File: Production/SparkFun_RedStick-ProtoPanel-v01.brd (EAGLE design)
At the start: 137.2 x 153.2 mm, 495 parts, among them Q1 DMG2307L, Q10 MOSFET-NCHANNEL2N7002PW, Q11 DMG2307L, Q12 MOSFET-NCHANNEL2N7002PW, Q13 DMG2307L, Q14 MOSFET-NCHANNEL2N7002PW, Q15 DMG2307L, Q16 MOSFET-NCHANNEL2N7002PW, Q17 DMG2307L, Q18 MOSFET-NCHANNEL2N7002PW, Q19 DMG2307L, Q2 MOSFET-NCHANNEL2N7002PW, Q20 MOSFET-NCHANNEL2N7002PW, Q21 DMG2307L, Q22 MOSFET-NCHANNEL2N7002PW, Q23 DMG2307L, Q24 MOSFET-NCHANNEL2N7002PW, Q3 DMG2307L, Q4 MOSFET-NCHANNEL2N7002PW, Q5 DMG2307L, Q6 MOSFET-NCHANNEL2N7002PW, Q7 DMG2307L, Q8 MOSFET-NCHANNEL2N7002PW, Q9 DMG2307L, U1 FTS31XS-U, U10 ATMEGA328P_TQFP, U11 5.0v, U12 FTS31XS-U, U13 ATMEGA328P_TQFP, U14 5.0v, U15 FTS31XS-U, U16 ATMEGA328P_TQFP, U17 5.0v, U18 FTS31XS-U, U19 ATMEGA328P_TQFP, U2 ATMEGA328P_TQFP, U20 5.0v, U21 FTS31XS-U, U22 ATMEGA328P_TQFP, U23 5.0v, U24 FTS31XS-U, U25 ATMEGA328P_TQFP, U26 5.0v, U27 FTS31XS-U, U28 ATMEGA328P_TQFP, U29 5.0v, U3 ATMEGA328P_TQFP, U30 FTS31XS-U, U31 ATMEGA328P_TQFP, U32 5.0v, U33 FTS31XS-U, U34 ATMEGA328P_TQFP, U35 5.0v, U36 FTS31XS-U, U4 5.0v, U5 5.0v, U6 FTS31XS-U, U7 ATMEGA328P_TQFP, U8 5.0v, U9 FTS31XS-U, Y1 16MHZ, Y10 16MHZ, Y11 16MHZ, Y12 16MHZ, Y2 16MHZ, Y3 16MHZ, Y4 16MHZ, Y5 16MHZ, Y6 16MHZ, Y7 16MHZ, Y8 16MHZ, Y9 16MHZ

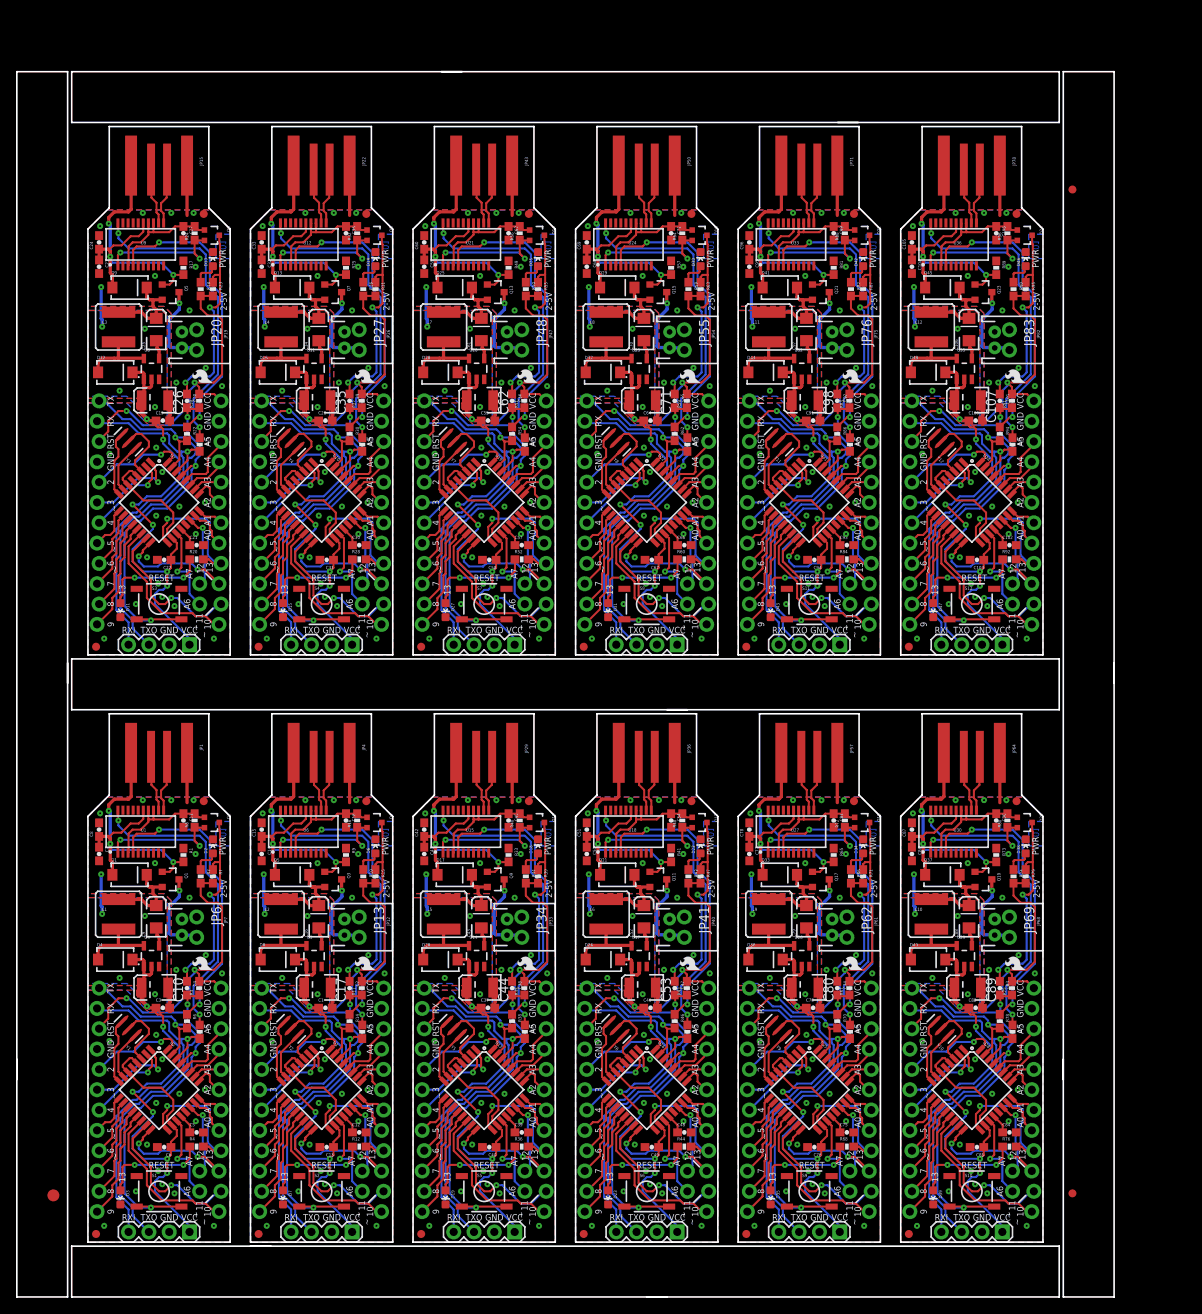
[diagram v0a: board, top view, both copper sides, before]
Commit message: added "route out" removed gerbers
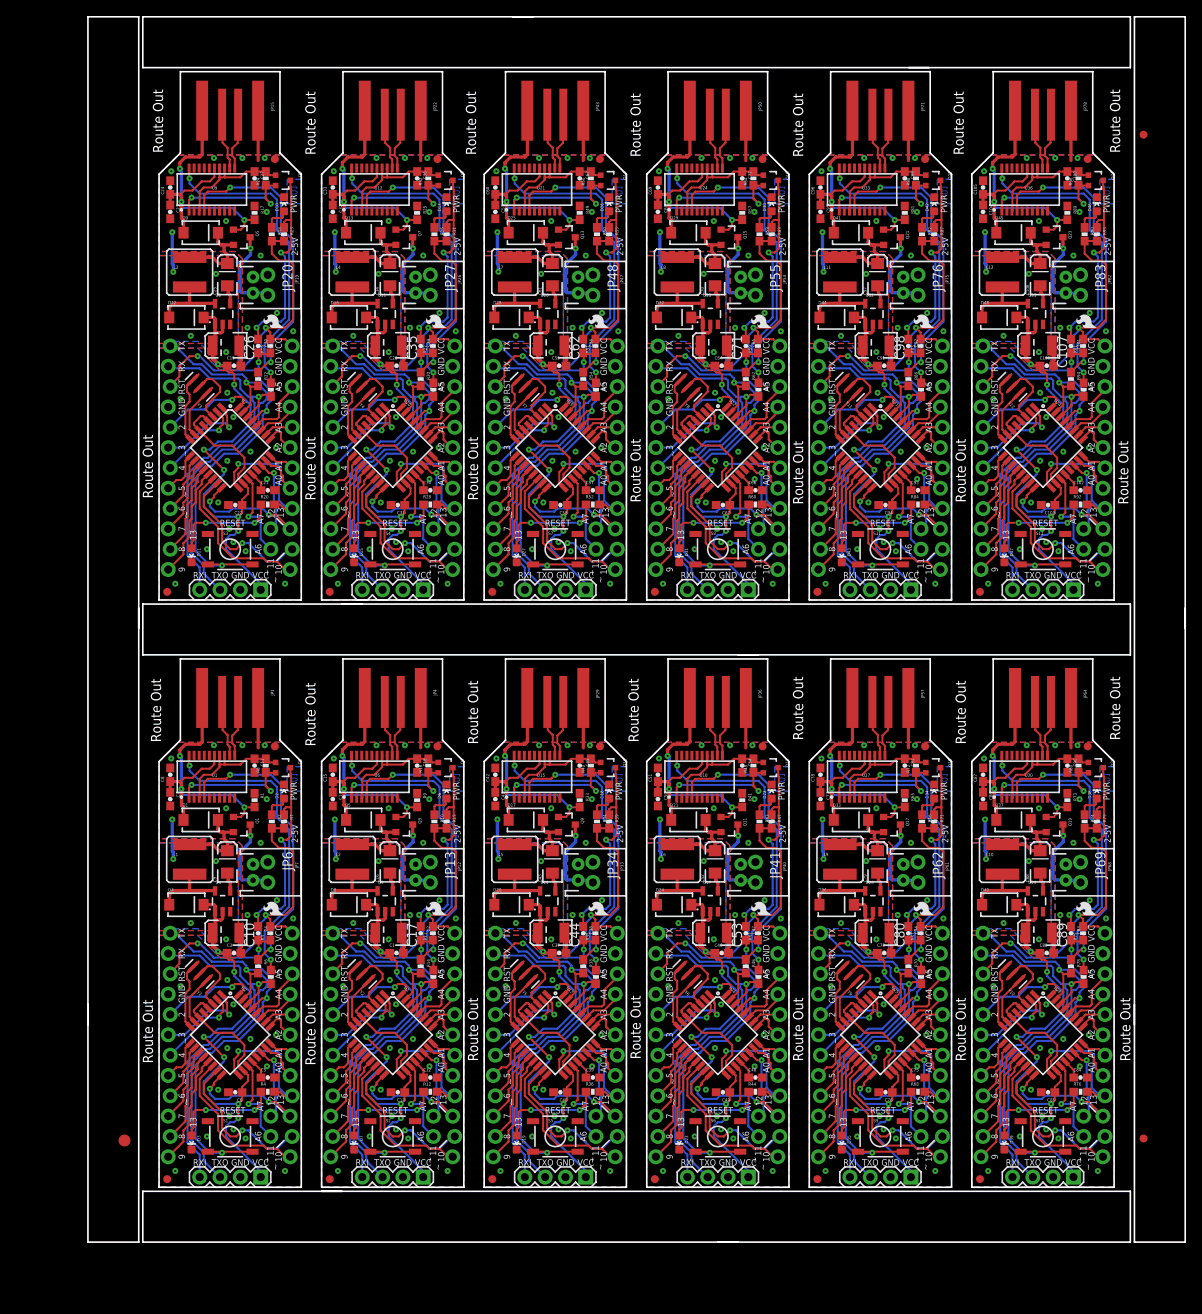
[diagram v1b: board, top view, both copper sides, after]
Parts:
- moved JP53 11.2 mm to (71.1, 84.1)
- moved LOGO13 11.2 mm to (65.5, 113.9)
- moved LOGO9 11.2 mm to (65.5, 40.5)
- moved JP31 11.2 mm to (66.0, 38.6)
- moved JP39 11.2 mm to (71.1, 10.7)
- moved C100 11.2 mm to (119.9, 109.6)
- moved C102 11.2 mm to (124.1, 94.0)
- moved C106 11.2 mm to (119.0, 120.9)
- moved C107 11.2 mm to (118.9, 112.1)
- moved C11 11.2 mm to (20.8, 59.6)
- moved C12 11.2 mm to (42.8, 20.6)
- moved C13 11.2 mm to (38.7, 18.7)
- moved C15 11.2 mm to (30.6, 58.4)
- moved C18 11.2 mm to (41.1, 59.6)
- moved C19 11.2 mm to (18.3, 109.6)
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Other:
- outline, holes or cut-outs redrawn
- board text added: "Route Out"
